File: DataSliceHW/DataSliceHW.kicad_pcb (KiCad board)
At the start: 2 copper layers, 85.5 x 54 mm, 161 parts, among them J1 USB4105-GF-A, J2 68712414522, J3 53261-0271, J4 DM3D-SF, Q1 BC847BDW1, Q2 FS8205A, SW1 K3-1391D-5MM, U1 ESP32-S3-WROOM-1, U2 CP2102N-A02-GQFN28, U3 AMS1117-3.3 / SGM2212-3.3, U4 DW01A, U5 TP4056-42-ESOP8, U6 MT3608/SX1308

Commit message: CC1101 progress
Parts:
- added C18: 100pF/50V(5%)NP0, Capacitor_SMD:C_0402_1005Metric_Pad0.74x0.62mm_HandSolder, B.Cu at (51.8, 35.8)
- added C20: 0.1uF/50V(10%)X5R, Capacitor_SMD:C_0402_1005Metric_Pad0.74x0.62mm_HandSolder, B.Cu at (51.8, 37.8)
- added C21: 12pF/50V(5%)NP0, Capacitor_SMD:C_0402_1005Metric_Pad0.74x0.62mm_HandSolder, B.Cu at (51.8, 39.8)
- added C22: 1.5pF/50V(5%)NP0, Capacitor_SMD:C_0402_1005Metric_Pad0.74x0.62mm_HandSolder, B.Cu at (51.8, 41.8)
- added C23: 1pF/50V(5%)NP0, Capacitor_SMD:C_0402_1005Metric_Pad0.74x0.62mm_HandSolder, B.Cu at (51.8, 43.7)
- added C24: 47pF/50V(5%)NP0, Capacitor_SMD:C_0402_1005Metric_Pad0.74x0.62mm_HandSolder, B.Cu at (51.8, 45.7)
- added C26: 3.3pF/50V(5%)NP0, Capacitor_SMD:C_0402_1005Metric_Pad0.74x0.62mm_HandSolder, B.Cu at (51.8, 47.7)
- added C27: 1.5pF/50V(5%)NP0, Capacitor_SMD:C_0402_1005Metric_Pad0.74x0.62mm_HandSolder, B.Cu at (51.8, 49.6)
- added J5: 66011102111302, Connector_Coaxial:WR-MMCX_Wuerth_66011102111302_Horizontal, B.Cu at (47.0, 38.0)
- added L2: 18nH(5%), Inductor_SMD:L_0402_1005Metric_Pad0.77x0.64mm_HandSolder, B.Cu at (55.0, 35.9)
- added L3: 12nH(5%), Inductor_SMD:L_0402_1005Metric_Pad0.77x0.64mm_HandSolder, B.Cu at (55.0, 37.8)
- added L4: 12nH(5%), Inductor_SMD:L_0402_1005Metric_Pad0.77x0.64mm_HandSolder, B.Cu at (55.0, 39.8)
- added L5: 12nH(5%), Inductor_SMD:L_0402_1005Metric_Pad0.77x0.64mm_HandSolder, B.Cu at (55.0, 41.8)
- added L6: 3.3nH(5%), Inductor_SMD:L_0402_1005Metric_Pad0.77x0.64mm_HandSolder, B.Cu at (55.0, 43.8)
- added L7: 12nH(5%), Inductor_SMD:L_0402_1005Metric_Pad0.77x0.64mm_HandSolder, B.Cu at (55.0, 45.8)
- added L8: 18nH(5%), Inductor_SMD:L_0402_1005Metric_Pad0.77x0.64mm_HandSolder, B.Cu at (55.0, 47.8)
- added R23: 56K(1%), Resistor_SMD:R_0402_1005Metric_Pad0.72x0.64mm_HandSolder, B.Cu at (55.0, 49.8)
- added U6: CC1101RGPR, Package_DFN_QFN:QFN-20-1EP_4x4mm_P0.5mm_EP2.5x2.5mm, B.Cu at (47.0, 46.8)
- moved SW1 35.7 mm to (80.8, 38.8), turned to 0 degrees
- moved J1 18.2 mm to (120.0, 39.0)
- moved D46 18.0 mm to (129.8, 85.8)
- moved D47 18.0 mm to (135.3, 85.8)
- moved C1 18.0 mm to (127.0, 41.8)
- moved C10 18.0 mm to (143.0, 51.2)
- moved C11 18.0 mm to (86.8, 48.8)
- moved C12 18.0 mm to (86.8, 50.8)
- moved C13 18.0 mm to (113.5, 43.5)
- moved C14 18.0 mm to (88.5, 49.2)
- moved C15 18.0 mm to (89.5, 49.2)
- moved C16 18.0 mm to (100.8, 41.5)
- moved C17 18.0 mm to (93.8, 49.8)
- moved C19 18.0 mm to (101.2, 38.2)
- moved C2 18.0 mm to (136.2, 51.2)
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- renumbered C21 to C10, C15 to C11, C17 to C12, C18 to C13, C16 to C15, C22 to C16, C23 to C17, C20 to C25, C10 to C28, C11 to C29, C12 to C30, C13 to C31, J4 to J2, J2 to J4, R20 to R10, R10 to R11, R11 to R12, R12 to R13, R13 to R19, R21 to R20, R22 to R21, R19 to R22, U4 to U3, U5 to U4, U6 to U5, U3 to U7

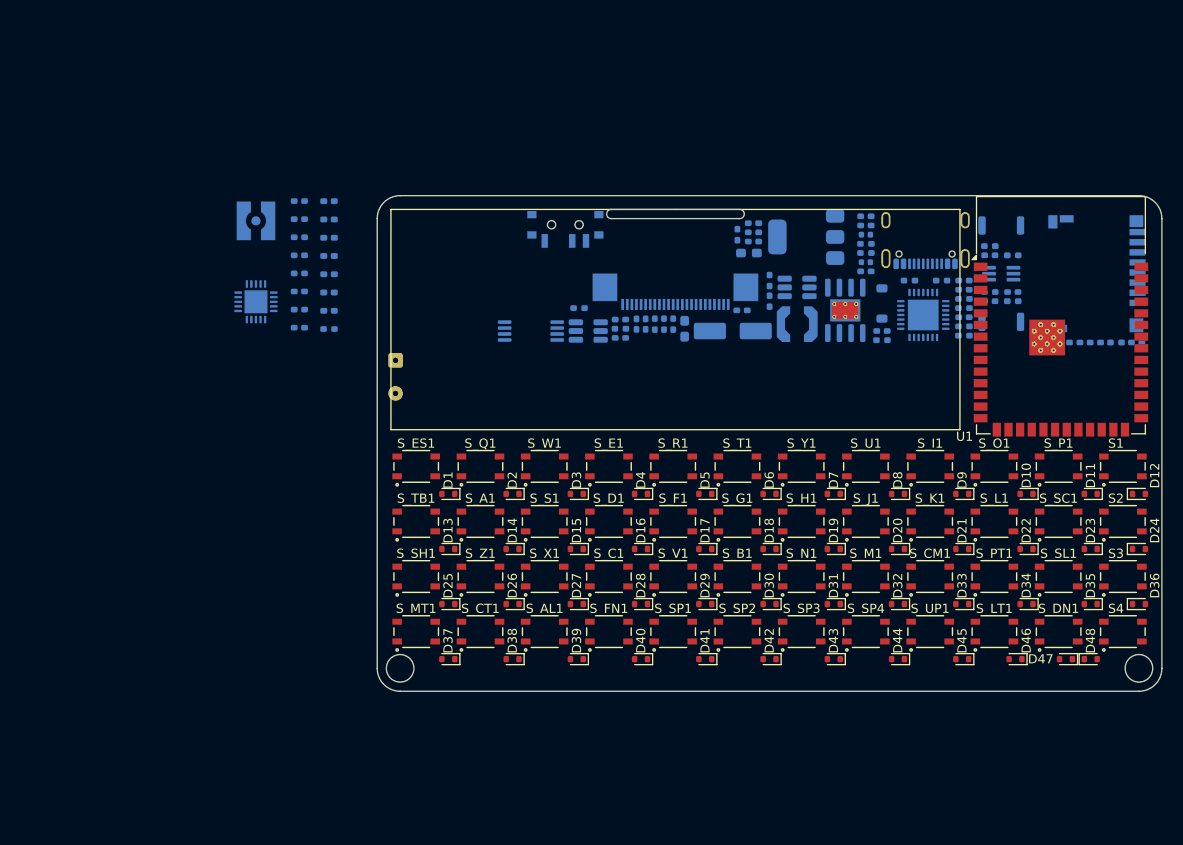
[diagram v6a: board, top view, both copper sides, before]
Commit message: Minor schematic changes and some PCB tracing progress
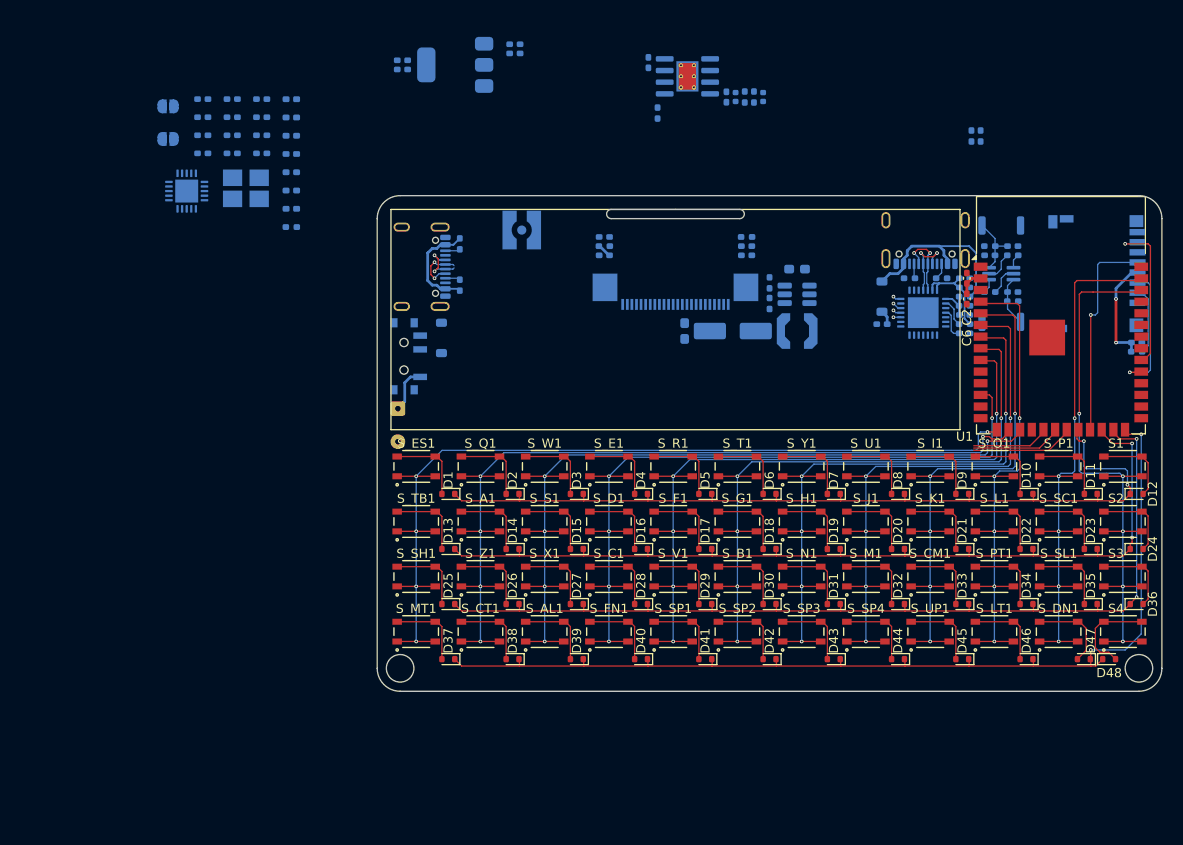
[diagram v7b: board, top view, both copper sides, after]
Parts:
- removed the C12 at (86.8, 50.8)
- removed the C21 at (51.8, 39.8)
- removed the C22 at (51.8, 41.8)
- removed the C27 at (51.8, 49.6)
- removed Q2: FS8205A, Package_SO:TSSOP-8_4.4x3mm_P0.65mm
- removed the R14 at (86.8, 49.8)
- removed the R16 at (82.2, 47.5)
- removed the U3 at (83.2, 50.0)
- added C25: 12pF(5%)NP0, Capacitor_SMD:C_0402_1005Metric_Pad0.74x0.62mm_HandSolder, B.Cu at (44.5, 24.7)
- added C28: 1pF(5%)NP0, Capacitor_SMD:C_0402_1005Metric_Pad0.74x0.62mm_HandSolder, B.Cu at (44.5, 28.7)
- added C29: 47pF(5%)NP0, Capacitor_SMD:C_0402_1005Metric_Pad0.74x0.62mm_HandSolder, B.Cu at (44.5, 30.6)
- added C30: 3.3pF(5%)NP0, Capacitor_SMD:C_0402_1005Metric_Pad0.74x0.62mm_HandSolder, B.Cu at (41.2, 24.7)
- added C31: 12pF(5%)NP0, Capacitor_SMD:C_0402_1005Metric_Pad0.74x0.62mm_HandSolder, B.Cu at (41.2, 26.7)
- added C33: 1.5pF(5%)NP0, Capacitor_SMD:C_0402_1005Metric_Pad0.74x0.62mm_HandSolder, B.Cu at (41.2, 28.7)
- added C34: 12pF(5%)NP0, Capacitor_SMD:C_0402_1005Metric_Pad0.74x0.62mm_HandSolder, B.Cu at (41.2, 30.6)
- added D53: 1N5819HW-7-F, Diode_SMD:D_SOD-123, B.Cu at (67.2, 50.8)
- added J6: USB4105-GF-A, Connector_USB:USB_C_Receptacle_GCT_USB4105-xx-A_16P_TopMnt_Horizontal, B.Cu at (64.0, 43.0)
- added R18: 5.1K(1%), Resistor_SMD:R_0402_1005Metric_Pad0.72x0.64mm_HandSolder, B.Cu at (69.2, 45.0)
- added R19: 5.1K(1%), Resistor_SMD:R_0402_1005Metric_Pad0.72x0.64mm_HandSolder, B.Cu at (69.2, 40.5)
- added R24: 0R, Jumper:SolderJumper-2_P1.3mm_Open_RoundedPad1.0x1.5mm, B.Cu at (37.5, 29.1)
- added R25: 56K(1%), Resistor_SMD:R_0402_1005Metric_Pad0.72x0.64mm_HandSolder, B.Cu at (50.9, 38.7)
- added Y1: 3225-26M-SR, Crystal:Crystal_SMD_3225-4Pin_3.2x2.5mm_HandSoldering, B.Cu at (45.9, 34.5)
- C1, C5, C8: value 1uF/16V(10%) -> 1uF(10%)
- C10: renamed from C28; value 10uF/25V(20%) -> 10uF(20%)
- C11: renamed from C29; value 0.1uF/50V(10%) -> 0.1uF(10%)
- C12: renamed from C30; value 0.1uF/50V(10%) -> 0.1uF(10%)
- C13: renamed from C31; value 10uF/25V(20%) -> 10uF(20%)
- C14: renamed from C10; value 0.1uF/50V(10%) -> 0.1uF(10%)
- C15: renamed from C13; value 0.1uF/50V(10%) -> 0.1uF(10%)
- C16: renamed from C11; value 10uF/25V(20%) -> 10uF(20%)
- C17: renamed from C14; value 4.7uF/16V(10%) -> 4.7uF(10%)
- C18: value 100pF/50V(5%)NP0 -> 1uF/50V(10%)
- C19: renamed from C15; value 0.1uF/50V(10%) -> 0.1uF(10%)
- C2: value 10uF/25V(20%) -> 10uF(20%); moved to F.Cu
- C20: value 0.1uF/50V(10%)X5R -> 0.1uF/50V(10%)
- C21: renamed from C16; value 22uF/50V(10%) -> 22uF(10%)
- C22: renamed from C17; value 22uF/50V(10%) -> 22uF(10%)
- C23: value 1pF/50V(5%)NP0 -> 100pF(5%)NP0
- C24: value 47pF/50V(5%)NP0 -> 0.1uF(10%)X5R
- C26: value 3.3pF/50V(5%)NP0 -> 1.5pF(5%)NP0
- C27: renamed from C19; value 4.7uF/50V(10%) -> 4.7uF(10%)
- C3, C4: value 10uF/25V(20%) -> 10uF(20%)
- C32: renamed from C25; value 4.7uF/50V(10%) -> 4.7uF(10%)
- C6: value 0.1uF/50V(10%) -> 0.1uF(10%); moved to F.Cu
- C7: value 4.7uF/16V(10%) -> 4.7uF(10%)
- C9: value 0.1uF/50V(10%) -> 0.1uF(10%)
- D50: value RED -> BLUE
- R23: value 56K(1%) -> 0R; footprint Resistor_SMD:R_0402_1005Metric_Pad0.72x0.64mm_HandSolder -> Jumper:SolderJumper-2_P1.3mm_Open_RoundedPad1.0x1.5mm
- moved C10 42.6 mm to (75.2, 19.8)
- moved C11 42.6 mm to (75.2, 18.8)
- moved C12 42.6 mm to (63.0, 21.5)
- moved C13 42.6 mm to (63.0, 20.5)
- moved U3 42.6 mm to (68.8, 21.0)
- moved R12 39.3 mm to (126.0, 28.8)
- moved R13 39.3 mm to (125.0, 28.8)
- moved R16 34.8 mm to (90.8, 26.2), turned to 90 degrees
- moved U4 30.8 mm to (94.0, 22.2), turned to 0 degrees
- moved R23 29.9 mm to (37.5, 25.5)
- moved J5 29.0 mm to (76.0, 39.0), turned to 0 degrees
- moved C16 28.2 mm to (89.8, 20.8), turned to 90 degrees
- moved C15 24.3 mm to (98.3, 24.5), turned to -90 degrees
- moved D51 22.9 mm to (99.3, 24.5), turned to 90 degrees
- moved SW1 22.2 mm to (63.5, 52.8), turned to 90 degrees
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- renumbered R17 to R14, R18 to R16, R19 to R17, U7 to U3
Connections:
- C10 pad 2: +4V -> +BATT
- C11 pad 1: +4V -> +BATT
- C15 pad 1: +5V -> GND
- C15 pad 2: GND -> +5V
- C16 pad 2: +4V -> +BATT
- C18 pad 1: Net-(C18-Pad1) -> GNDA
- C18 pad 2: GNDA -> VDDA
- C20 pad 1: Net-(U6-DCOUPL) -> VDDA
- C23 pad 1: Net-(C22-Pad1) -> Net-(C23-Pad1)
- C23 pad 2: Net-(C23-Pad2) -> GNDA
- C24 pad 1: Net-(C21-Pad1) -> Net-(U6-DCOUPL)
- C24 pad 2: Net-(C24-Pad2) -> GNDA
- C26 pad 2: GNDA -> Net-(C26-Pad2)
- J3 pad 1: Net-(J3-Pin_1) -> +4V
- J3 pad 2: -BATT -> GND
- L2 pad 1: Net-(C22-Pad1) -> Net-(C26-Pad1)
- L2 pad 2: Net-(C18-Pad1) -> Net-(C23-Pad1)
- L3 pad 2: Net-(C22-Pad1) -> Net-(C26-Pad1)
- L4 pad 1: Net-(C22-Pad2) -> Net-(C26-Pad2)
- L4 pad 2: Net-(C26-Pad1) -> Net-(C30-Pad1)
- L5 pad 1: Net-(C26-Pad1) -> Net-(C30-Pad1)
- L5 pad 2: Net-(C21-Pad1) -> Net-(C25-Pad1)
- L6 pad 2: Net-(C24-Pad2) -> Net-(C29-Pad2)
- L7 pad 1: Net-(C23-Pad2) -> Net-(C28-Pad2)
- L8 pad 1: Net-(C22-Pad2) -> Net-(C26-Pad2)
- L8 pad 2: Net-(C23-Pad2) -> Net-(C28-Pad2)
- R15 pad 1: Net-(U4-~{CHRG}) -> Net-(D51-K)
- R15 pad 2: Net-(D51-K) -> Net-(U4-~{CHRG})
- R16 pad 1: GND -> Net-(U4-PROG)
- R16 pad 2: Net-(U4-PROG) -> GND
- R23 pad 1: Net-(U6-RBIAS) -> VDDA
- R23 pad 2: GNDA -> VCC
- SW1 pad 1: Net-(J3-Pin_1) -> +4V
- SW1 pad 2: +4V -> +BATT
- U1 pad 12: /KB_C_7 -> /KB_C_3
- U1 pad 15: /KB_C_2 -> /KB_C_0
- U1 pad 16: /KB_R_1 -> /KB_C_1
- U1 pad 17: /KB_C_8 -> /KB_C_2
- U1 pad 22: /KB_C_9 -> /KB_R_0
- U1 pad 24: /KB_R_2 -> /KB_R_1
- U1 pad 25: /KB_R_3 -> /KB_R_2
- U1 pad 26: /KB_R_0 -> /KB_R_3
- U1 pad 33: unconnected-(U1-IO40-Pad33) -> /SUB_CS
- U1 pad 38: /KB_C_1 -> /KB_C_11
- U1 pad 39: /KB_C_0 -> /KB_C_10
- U1 pad 4: /KB_C_3 -> /KB_C_9
- U1 pad 5: /KB_C_4 -> /KB_C_8
- U1 pad 6: /KB_C_5 -> /KB_C_7
- U1 pad 8: /KB_C_10 -> /KB_C_5
- U1 pad 9: /KB_C_11 -> /KB_C_4
- U3 pad 3: +4V -> +BATT
- U4 pad 5: +4V -> +BATT
- U6 pad 10: unconnected-(U6-XOSC_Q2-Pad10) -> Net-(U6-XOSC_Q2)
- U6 pad 7: unconnected-(U6-CSN-Pad7) -> /SUB_CS
- U6 pad 8: unconnected-(U6-XOSC_Q1-Pad8) -> Net-(U6-XOSC_Q1)
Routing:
- net /KB_R_3: track 0.00 -> 109.7 mm, vias 0 -> 2
- net /KB_R_2: track 0.00 -> 103.3 mm, vias 0 -> 2
- net /KB_C_0: track 0.00 -> 101.2 mm, vias 0 -> 5
- net /KB_R_1: track 0.00 -> 97.7 mm, vias 0 -> 2
- net /KB_C_1: track 0.00 -> 96.4 mm, vias 0 -> 5
- net /KB_R_0: track 0.00 -> 94.3 mm, vias 0 -> 2
- net /KB_C_2: track 0.00 -> 89.5 mm, vias 0 -> 5
- net /KB_C_3: track 0.00 -> 84.9 mm, vias 0 -> 5
- net /KB_C_4: track 0.00 -> 82.9 mm, vias 0 -> 5
- net /KB_C_5: track 0.00 -> 78.3 mm, vias 0 -> 5
- net /KB_C_6: track 0.00 -> 73.7 mm, vias 0 -> 5
- net /KB_C_7: track 0.00 -> 69.1 mm, vias 0 -> 5
- net /KB_C_11: track 0.00 -> 65.8 mm, vias 0 -> 5
- net /KB_C_10: track 0.00 -> 64.6 mm, vias 0 -> 5
- net /KB_C_8: track 0.00 -> 64.5 mm, vias 0 -> 5
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
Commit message: PCB progress
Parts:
- moved R12 27.7 mm to (140.8, 52.2), turned to 0 degrees
- moved R13 27.5 mm to (140.8, 51.2), turned to 0 degrees
- moved R16 2.94 mm to (89.8, 23.5), turned to -90 degrees
- moved C5 2.50 mm to (127.0, 40.8), turned to 180 degrees
- moved R2 2.50 mm to (129.5, 40.8), turned to 180 degrees
- moved C14 1.00 mm to (143.0, 52.2)
- moved R10 1.00 mm to (143.0, 51.2)
- moved C16 0.25 mm to (89.8, 21.0)
- moved C2 0.25 mm to (124.5, 44.5)
- moved C6 0.25 mm to (124.5, 46.8)
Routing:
- net VCC: track 26.0 -> 116.9 mm
- net /I2C_SDA: track 0.00 -> 73.1 mm, vias 0 -> 3
- net /I2C_SCL: track 0.00 -> 72.1 mm, vias 0 -> 3
- net /UART_TX: track 0.90 -> 45.5 mm, vias 1 -> 3
- net /UART_RX: track 1.01 -> 45.3 mm, vias 1 -> 3
- net /GPIO0: track 5.46 -> 34.1 mm, vias 0 -> 3
- net /RTS: track 2.36 -> 30.1 mm, vias 1 -> 2
- net /DTR: track 2.47 -> 26.7 mm, vias 1 -> 2
- net /ESP_EN: track 6.79 -> 21.1 mm, vias 0 -> 1
- net /OLED_RST: track 0.00 -> 12.6 mm
- net Net-(J4-Pad21): track 0.00 -> 10.1 mm
- net Net-(C27-Pad2): track 0.00 -> 8.64 mm
- net /SD_CLK: track 23.1 -> 24.2 mm, vias 1 -> 3
- net Net-(J2-DAT3/CD): track 7.45 -> 6.45 mm
- net /KB_C_11: track 65.8 -> 66.3 mm
